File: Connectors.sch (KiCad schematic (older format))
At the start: 16 parts, among them J1 Conn_01x02, J10 Conn_01x08, J11 Conn_01x03, J12 Conn_01x02, J14 Conn_01x04, J15 Conn_01x04, J16 Conn_01x01, J17 Conn_01x04, J2 Conn_01x04, J3 Conn_01x04, J4 Conn_01x03, J5 Conn_01x03, J6 Conn_01x06, J7 Conn_01x06, J8 Conn_01x04, J9 Conn_01x08

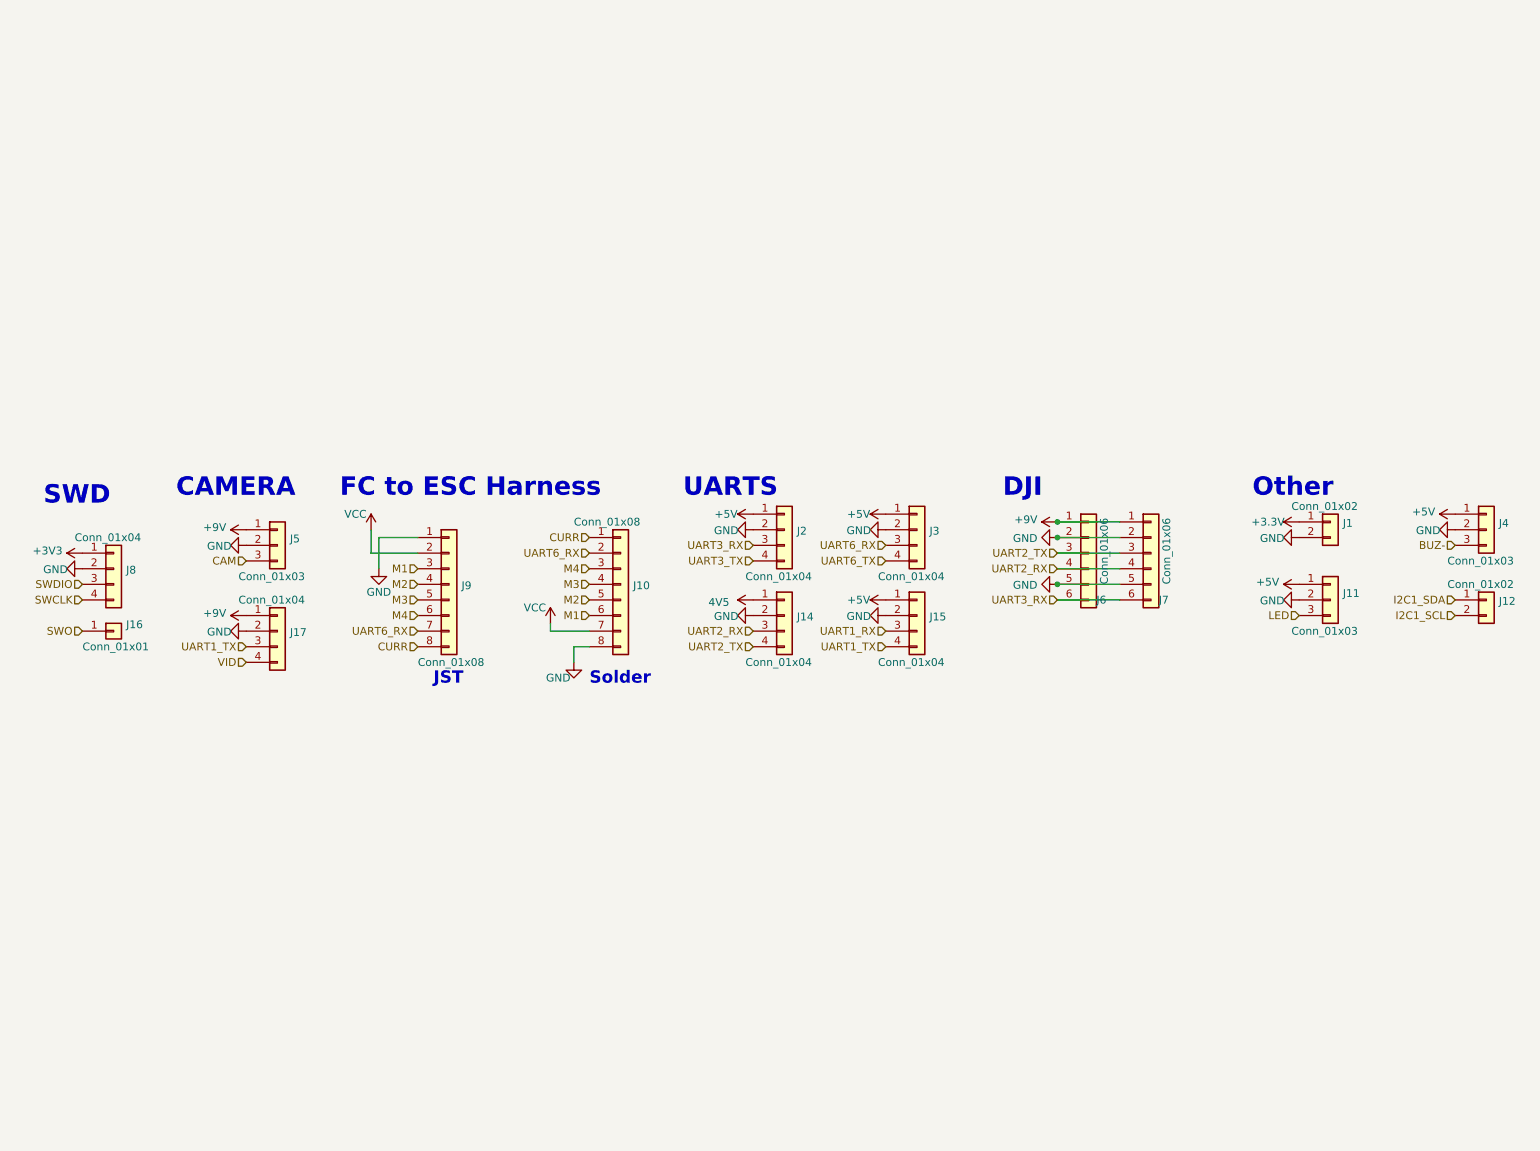
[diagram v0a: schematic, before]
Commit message: Updated the schematics to include pictures
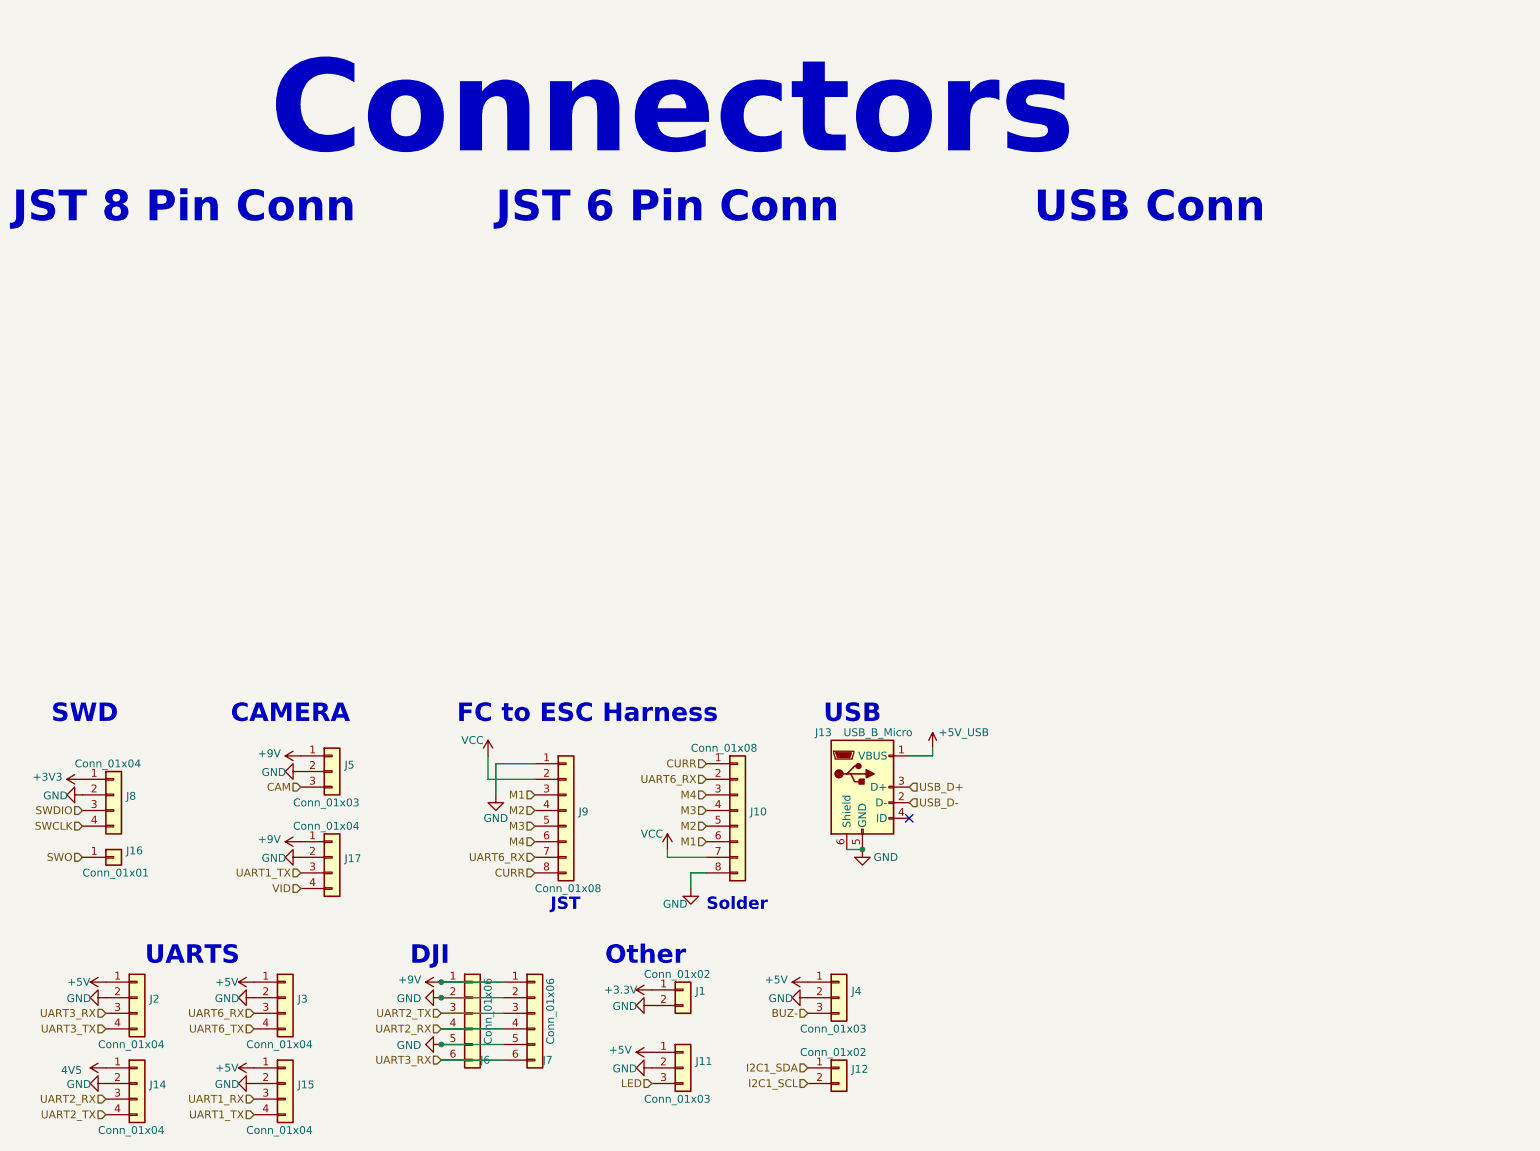
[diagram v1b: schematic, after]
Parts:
- added J13: USB_B_Micro, Connector_USB:USB_Micro-B_Amphenol_10103594-0001LF_Horizontal, symbol Connector:USB_B_Micro
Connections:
- net GND: now also J13.5 (GND), J13.6 (Shield)
- new net +5V_USB: J13.1 (VBUS)
- new net USB_D+: J13.3 (D+)
- new net USB_D-: J13.2 (D-)
- no-connect marks 0 -> 1
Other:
- note added: "Connectors"
- note added: "JST 6 Pin Conn"
- note added: "JST 8 Pin Conn"
- note added: "USB"
- note added: "USB Conn"
- moved on the sheet: J1, J10, J11, J12, J14, J15, J16, J17, J2, J3, J4, J5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

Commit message: Changed around routing
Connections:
- net CURR: now also J10.3 (Pin_3), J9.3 (Pin_3); no longer J10.1 (Pin_1), J9.8 (Pin_8)
- net GND: now also J10.2 (Pin_2), J9.2 (Pin_2); no longer J10.8 (Pin_8), J9.1 (Pin_1)
- net M1: now also J10.5 (Pin_5), J9.5 (Pin_5); no longer J10.6 (Pin_6), J9.3 (Pin_3)
- net M2: now also J10.6 (Pin_6), J9.6 (Pin_6); no longer J10.5 (Pin_5), J9.4 (Pin_4)
- net M3: now also J10.7 (Pin_7), J9.7 (Pin_7); no longer J10.4 (Pin_4), J9.5 (Pin_5)
- net M4: now also J10.8 (Pin_8), J9.8 (Pin_8); no longer J10.3 (Pin_3), J9.6 (Pin_6)
- net UART6_RX: now also J10.4 (Pin_4), J9.4 (Pin_4); no longer J10.2 (Pin_2), J9.7 (Pin_7)
- net VCC: now also J10.1 (Pin_1), J9.1 (Pin_1); no longer J10.7 (Pin_7), J9.2 (Pin_2)
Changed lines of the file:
@@
 CAMERA
 $Comp
-L power:VCC #PWR?
-U 1 1 60A865C1
-P 4000 5100
-AR Path="/60A865C1" Ref="#PWR?"  Part="1"
-AR Path="/60A7361B/60A865C1" Ref="#PWR0140"  Part="1"
-F 0 "#PWR0140" H 4000 4950 50  0001 C CNN
-F 1 "VCC" H 3900 5200 50  0000 C CNN
-F 2 "" H 4000 5100 50  0001 C CNN
-F 3 "" H 4000 5100 50  0001 C CNN
-	1    4000 5100
-	1    0    0    -1
-$EndComp
-$Comp
 L Connector_Generic:Conn_01x08 J?
 U 1 1 60A865C9
@@
 	3700 7050 4100 7050
 $Comp
-L power:GND #PWR?
-U 1 1 60A86572
-P 5300 5950
-AR Path="/60A86572" Ref="#PWR?"  Part="1"
-AR Path="/60A7361B/60A86572" Ref="#PWR0154"  Part="1"
-F 0 "#PWR0154" H 5300 5700 50  0001 C CNN
-F 1 "GND" H 5200 5850 50  0000 C CNN
-F 2 "" H 5300 5950 50  0001 C CNN
-F 3 "" H 5300 5950 50  0001 C CNN
-	1    5300 5950
-	1    0    0    -1
-$EndComp
-$Comp
-L power:VCC #PWR?
-U 1 1 60A8656C
-P 5150 5700
-AR Path="/60A8656C" Ref="#PWR?"  Part="1"
-AR Path="/60A7361B/60A8656C" Ref="#PWR0155"  Part="1"
-F 0 "#PWR0155" H 5150 5550 50  0001 C CNN
-F 1 "VCC" H 5050 5800 50  0000 C CNN
-F 2 "" H 5150 5700 50  0001 C CNN
-F 3 "" H 5150 5700 50  0001 C CNN
-	1    5150 5700
-	1    0    0    -1
-$EndComp
-$Comp
 L Connector_Generic:Conn_01x08 J?
 U 1 1 60A86564
@@
 	1    0    0    -1
 $EndComp
-$Comp
-L power:GND #PWR?
-U 1 1 60A865BB
-P 4050 5350
-AR Path="/60A865BB" Ref="#PWR?"  Part="1"
-AR Path="/60A7361B/60A865BB" Ref="#PWR0156"  Part="1"
-F 0 "#PWR0156" H 4050 5100 50  0001 C CNN
-F 1 "GND" H 4050 5200 50  0000 C CNN
-F 2 "" H 4050 5350 50  0001 C CNN
-F 3 "" H 4050 5350 50  0001 C CNN
-	1    4050 5350
-	1    0    0    -1
-$EndComp
-Wire Wire Line
-	4000 5250 4300 5250
-Wire Wire Line
-	4050 5350 4050 5150
-Wire Wire Line
-	4050 5150 4300 5150
-Wire Wire Line
-	4000 5100 4000 5250
-Text HLabel 4300 5450 0    50   Input ~ 0
-M2
-Text HLabel 4300 5350 0    50   Input ~ 0
-M1
-Text HLabel 4300 5550 0    50   Input ~ 0
-M3
-Text HLabel 4300 5650 0    50   Input ~ 0
-M4
-Text HLabel 4300 5750 0    50   Input ~ 0
-UART6_RX
-Text HLabel 4300 5850 0    50   Input ~ 0
-CURR
-Text HLabel 5400 5650 0    50   Input ~ 0
-M1
-Text HLabel 5400 5550 0    50   Input ~ 0
-M2
-Text HLabel 5400 5450 0    50   Input ~ 0
-M3
-Text HLabel 5400 5350 0    50   Input ~ 0
-M4
-Text HLabel 5400 5250 0    50   Input ~ 0
-UART6_RX
-Text HLabel 5400 5150 0    50   Input ~ 0
-CURR
-Wire Wire Line
-	5300 5950 5300 5850
-Wire Wire Line
-	5300 5850 5400 5850
-Wire Wire Line
-	5150 5700 5150 5750
-Wire Wire Line
-	5150 5750 5400 5750
 Text HLabel 2800 5300 0    50   Input ~ 0
 CAM
@@
 Text Notes 2600 1300 0    591  ~ 118
 Connectors
+$Comp
+L power:VCC #PWR?
+U 1 1 60DC538C
+P 5300 5050
+AR Path="/60DC538C" Ref="#PWR?"  Part="1"
+AR Path="/60A7361B/60DC538C" Ref="#PWR0154"  Part="1"
+F 0 "#PWR0154" H 5300 4900 50  0001 C CNN
+F 1 "VCC" H 5200 5150 50  0000 C CNN
+F 2 "" H 5300 5050 50  0001 C CNN
+F 3 "" H 5300 5050 50  0001 C CNN
+	1    5300 5050
+	1    0    0    -1
+$EndComp
+$Comp
+L power:GND #PWR?
+U 1 1 60DC5392
+P 4900 5350
+AR Path="/60DC5392" Ref="#PWR?"  Part="1"
+AR Path="/60A7361B/60DC5392" Ref="#PWR0155"  Part="1"
+F 0 "#PWR0155" H 4900 5100 50  0001 C CNN
+F 1 "GND" H 4900 5200 50  0000 C CNN
+F 2 "" H 4900 5350 50  0001 C CNN
+F 3 "" H 4900 5350 50  0001 C CNN
+	1    4900 5350
+	1    0    0    -1
+$EndComp
+Text HLabel 5400 5650 0    50   Input ~ 0
+M2
+Text HLabel 5400 5550 0    50   Input ~ 0
+M1
+Text HLabel 5400 5750 0    50   Input ~ 0
+M3
+Text HLabel 5400 5850 0    50   Input ~ 0
+M4
+Text HLabel 5400 5450 0    50   Input ~ 0
+UART6_RX
+Text HLabel 5400 5350 0    50   Input ~ 0
+CURR
+Wire Wire Line
+	5300 5050 5300 5150
+Wire Wire Line
+	5300 5150 5400 5150
+Wire Wire Line
+	4900 5250 4900 5350
+Wire Wire Line
+	4900 5250 5400 5250
+$Comp
+L power:VCC #PWR?
+U 1 1 60DD5891
+P 4200 5050
+AR Path="/60DD5891" Ref="#PWR?"  Part="1"
+AR Path="/60A7361B/60DD5891" Ref="#PWR0140"  Part="1"
+F 0 "#PWR0140" H 4200 4900 50  0001 C CNN
+F 1 "VCC" H 4100 5150 50  0000 C CNN
+F 2 "" H 4200 5050 50  0001 C CNN
+F 3 "" H 4200 5050 50  0001 C CNN
+	1    4200 5050
+	1    0    0    -1
+$EndComp
+$Comp
+L power:GND #PWR?
+U 1 1 60DD5897
+P 3800 5350
+AR Path="/60DD5897" Ref="#PWR?"  Part="1"
+AR Path="/60A7361B/60DD5897" Ref="#PWR0156"  Part="1"
+F 0 "#PWR0156" H 3800 5100 50  0001 C CNN
+F 1 "GND" H 3800 5200 50  0000 C CNN
+F 2 "" H 3800 5350 50  0001 C CNN
+F 3 "" H 3800 5350 50  0001 C CNN
+	1    3800 5350
+	1    0    0    -1
+$EndComp
+Text HLabel 4300 5650 0    50   Input ~ 0
+M2
+Text HLabel 4300 5550 0    50   Input ~ 0
+M1
+Text HLabel 4300 5750 0    50   Input ~ 0
+M3
+Text HLabel 4300 5850 0    50   Input ~ 0
+M4
+Text HLabel 4300 5450 0    50   Input ~ 0
+UART6_RX
+Text HLabel 4300 5350 0    50   Input ~ 0
+CURR
+Wire Wire Line
+	4200 5050 4200 5150
+Wire Wire Line
+	4200 5150 4300 5150
+Wire Wire Line
+	3800 5250 3800 5350
+Wire Wire Line
+	3800 5250 4300 5250
 $EndSCHEMATC
